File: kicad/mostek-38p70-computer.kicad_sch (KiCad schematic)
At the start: 7 parts

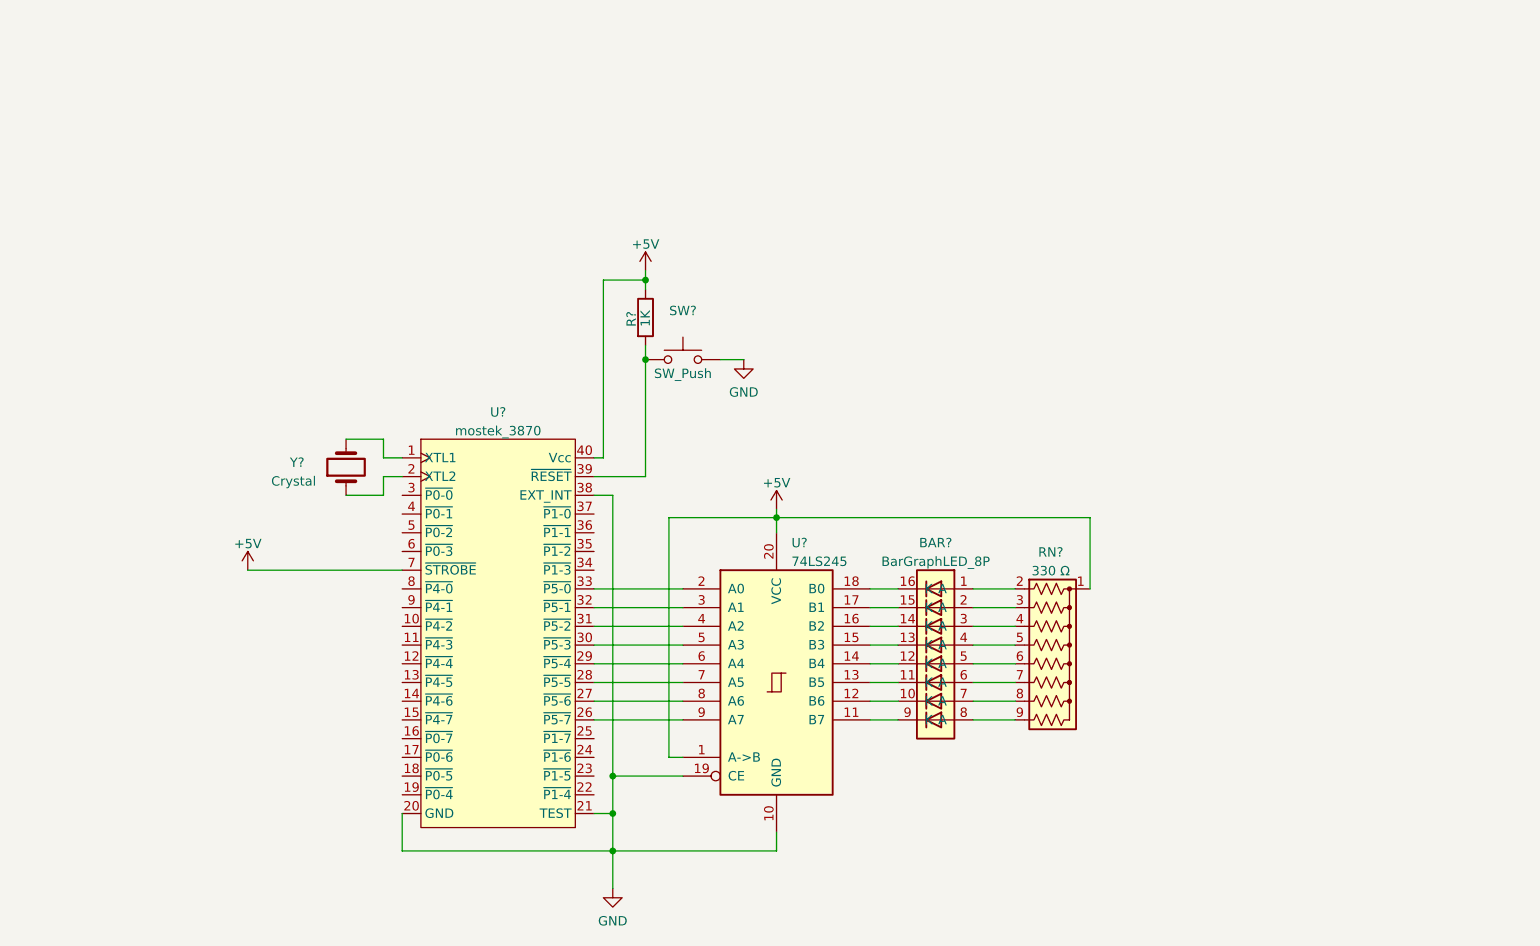
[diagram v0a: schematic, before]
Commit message: added switch inputs
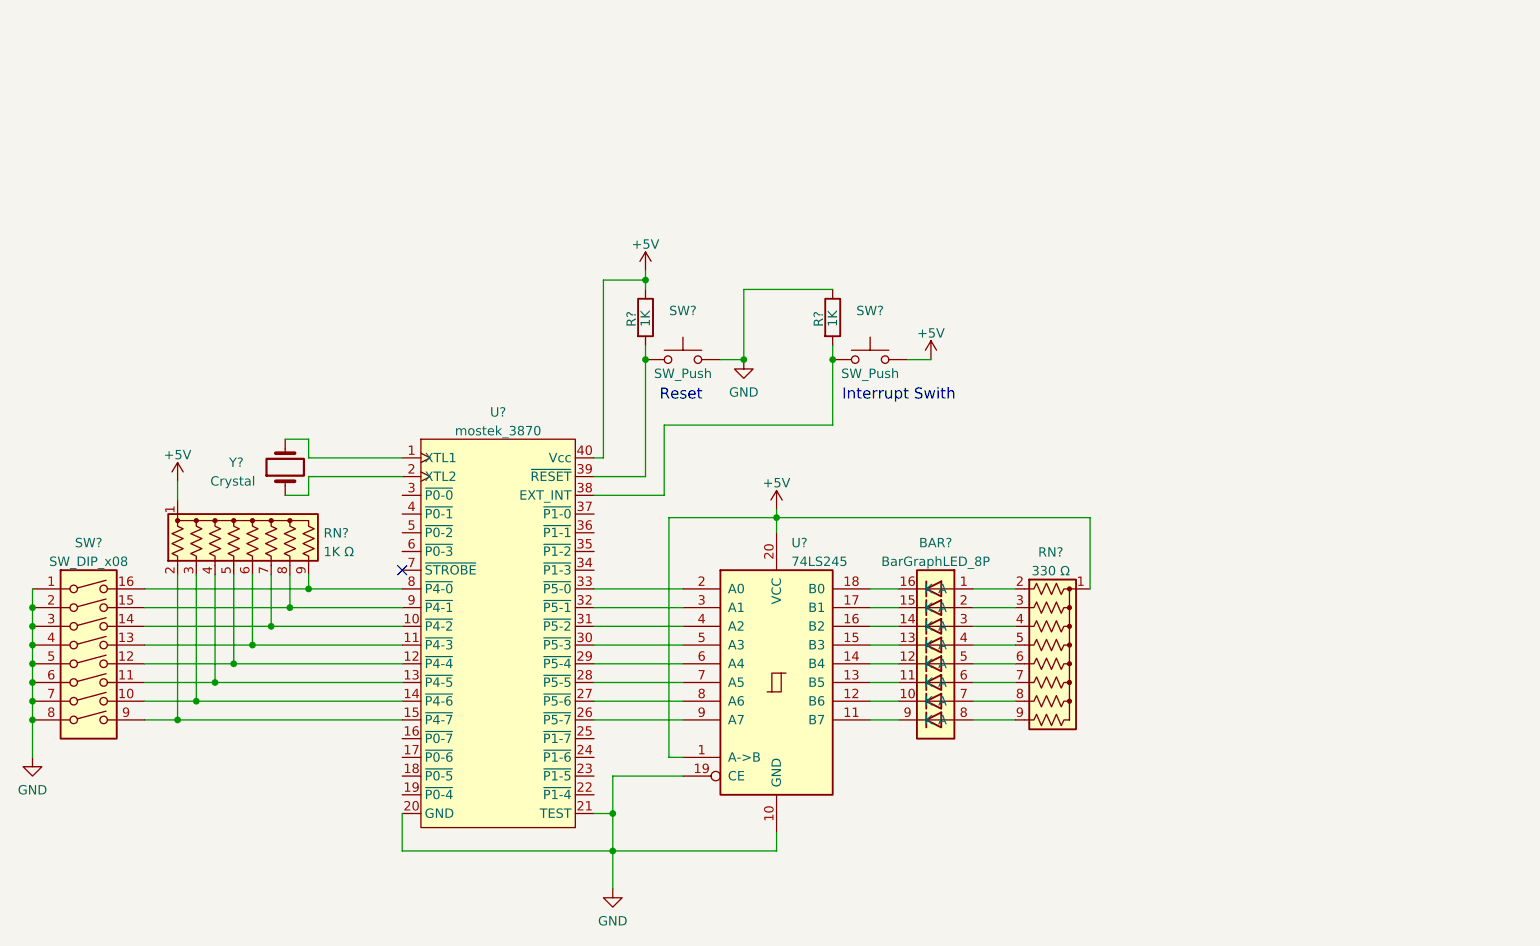
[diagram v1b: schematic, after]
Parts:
- added R?: 1K, symbol Device:R
- added RN?: 1K Ω, Resistor_THT:R_Array_SIP9, symbol Device:R_Network08_US
- added SW?: SW_DIP_x08, symbol Switch:SW_DIP_x08
- added SW?: SW_Push, symbol Switch:SW_Push
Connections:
- net +5V: now also RN?.1 (common), SW?.2; no longer U?.7 (~{STROBE})
- net GND: now also R?.1, SW?.1, SW?.2, SW?.3, SW?.4, SW?.5, SW?.6, SW?.7, SW?.8; no longer U?.38 (EXT_INT)
- net at U?.10 (~{P4-2}): now also RN?.7 (R6), SW?.14
- net at U?.11 (~{P4-3}): now also RN?.6 (R5), SW?.13
- net at U?.12 (~{P4-4}): now also RN?.5 (R4), SW?.12
- net at U?.13 (~{P4-5}): now also RN?.4 (R3), SW?.11
- net at U?.14 (~{P4-6}): now also RN?.3 (R2), SW?.10
- net at U?.15 (~{P4-7}): now also RN?.2 (R1), SW?.9
- net at U?.8 (~{P4-0}): now also RN?.9 (R8), SW?.16
- net at U?.9 (~{P4-1}): now also RN?.8 (R7), SW?.15
- new net: R?.2, SW?.1, U?.38 (EXT_INT)
- no-connect marks 0 -> 1
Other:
- note added: "Interrupt Swith"
- note added: "Reset"
- moved on the sheet: Y?

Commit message: added keypad to schematic
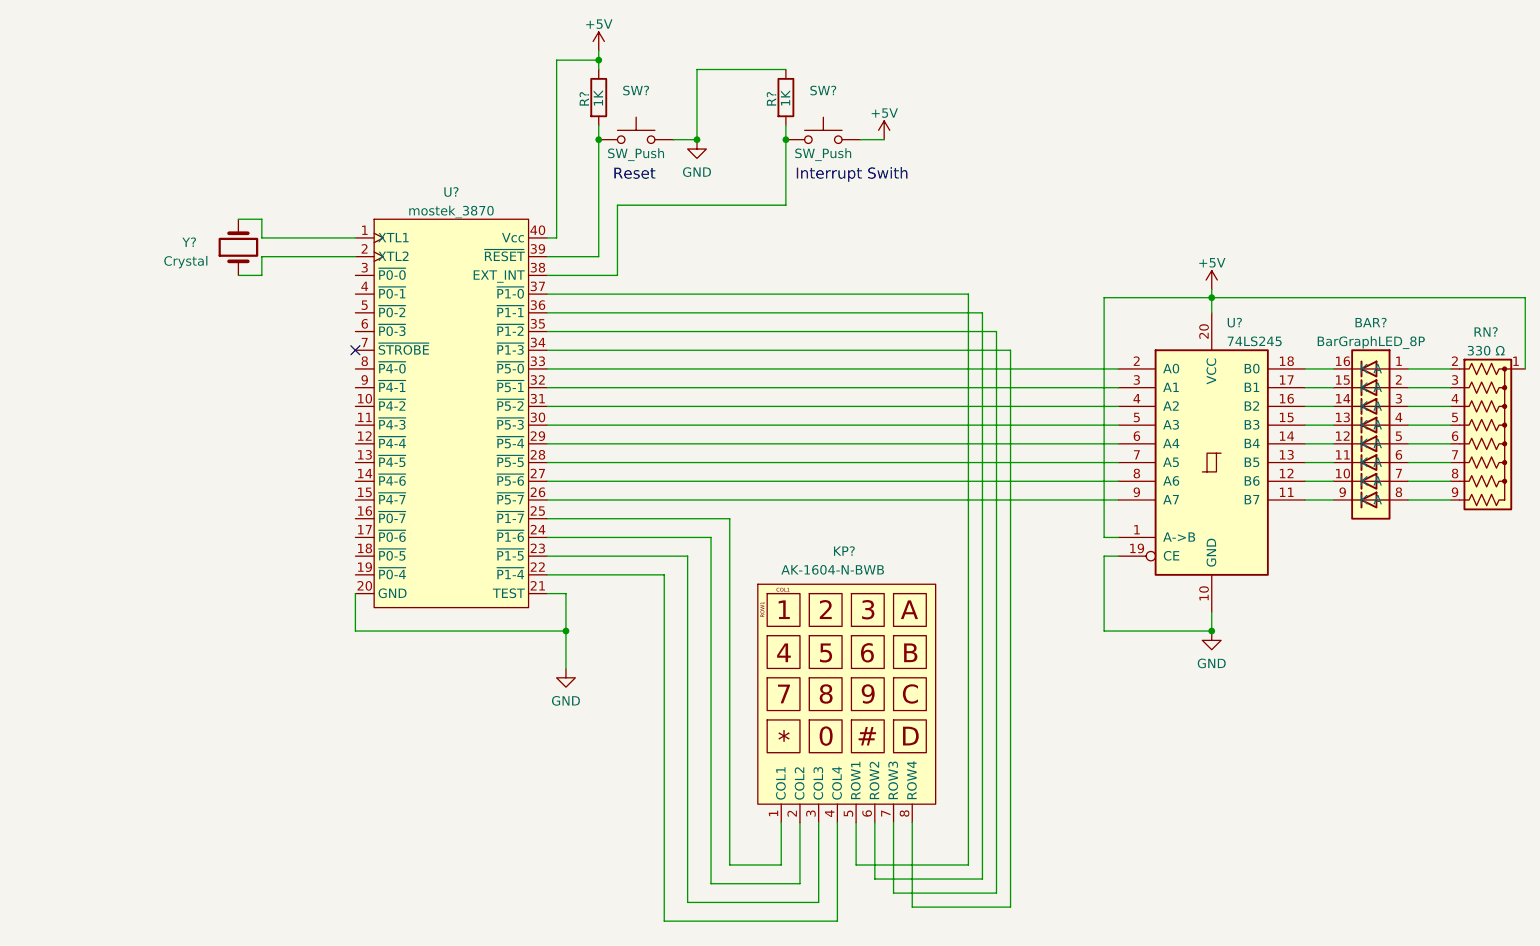
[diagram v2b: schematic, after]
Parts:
- removed RN?: 1K Ω, Resistor_THT:R_Array_SIP9, symbol Device:R_Network08_US
- removed SW?: SW_DIP_x08, symbol Switch:SW_DIP_x08
- added KP?: AK-1604-N-BWB, symbol ak_1604_keypad:AK-1604-N-BWB
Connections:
- net at U?.22 (~{P1-4}): now also KP?.4 (COL4)
- net at U?.23 (~{P1-5}): now also KP?.3 (COL3)
- net at U?.24 (~{P1-6}): now also KP?.2 (COL2)
- net at U?.25 (~{P1-7}): now also KP?.1 (COL1)
- net at U?.34 (~{P1-3}): now also KP?.8 (ROW4)
- net at U?.35 (~{P1-2}): now also KP?.7 (ROW3)
- net at U?.36 (~{P1-1}): now also KP?.6 (ROW2)
- net at U?.37 (~{P1-0}): now also KP?.5 (ROW1)
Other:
- moved on the sheet: BAR?, R?, RN?, SW?, U?, Y?

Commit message: added support for a keypad
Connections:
- net at KP?.1 (COL1): now also U?.22 (~{P1-4}); no longer U?.25 (~{P1-7})
- net at KP?.2 (COL2): now also U?.23 (~{P1-5}); no longer U?.24 (~{P1-6})
- net at KP?.3 (COL3): now also U?.24 (~{P1-6}); no longer U?.23 (~{P1-5})
- net at KP?.4 (COL4): now also U?.25 (~{P1-7}); no longer U?.22 (~{P1-4})
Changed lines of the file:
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@@
     (stroke (width 0) (type default) (color 0 0 0 0))
   )
-  (wire (pts (xy 160.655 130.81) (xy 167.64 130.81))
+  (wire (pts (xy 160.655 130.81) (xy 175.26 130.81))
     (stroke (width 0) (type default) (color 0 0 0 0))
   )
@@
     (stroke (width 0) (type default) (color 0 0 0 0))
   )
+  (wire (pts (xy 172.72 133.35) (xy 172.72 125.095))
+    (stroke (width 0) (type default) (color 0 0 0 0))
+  )
   (wire (pts (xy 252.73 81.28) (xy 258.445 81.28))
     (stroke (width 0) (type default) (color 0 0 0 0))
@@
     (stroke (width 0) (type default) (color 0 0 0 0))
   )
-  (wire (pts (xy 151.765 138.43) (xy 175.26 138.43))
+  (wire (pts (xy 167.64 138.43) (xy 167.64 125.095))
     (stroke (width 0) (type default) (color 0 0 0 0))
   )
@@
     (stroke (width 0) (type default) (color 0 0 0 0))
   )
+  (wire (pts (xy 154.94 135.89) (xy 170.18 135.89))
+    (stroke (width 0) (type default) (color 0 0 0 0))
+  )
   (wire (pts (xy 137.16 45.72) (xy 137.16 21.59))
     (stroke (width 0) (type default) (color 0 0 0 0))
@@
     (stroke (width 0) (type default) (color 0 0 0 0))
   )
-  (wire (pts (xy 154.94 135.89) (xy 172.72 135.89))
-    (stroke (width 0) (type default) (color 0 0 0 0))
-  )
   (wire (pts (xy 198.755 136.525) (xy 185.42 136.525))
     (stroke (width 0) (type default) (color 0 0 0 0))
@@
     (stroke (width 0) (type default) (color 0 0 0 0))
   )
+  (wire (pts (xy 170.18 135.89) (xy 170.18 125.095))
+    (stroke (width 0) (type default) (color 0 0 0 0))
+  )
   (wire (pts (xy 213.36 88.9) (xy 211.455 88.9))
     (stroke (width 0) (type default) (color 0 0 0 0))
@@
     (stroke (width 0) (type default) (color 0 0 0 0))
   )
-  (wire (pts (xy 170.18 133.35) (xy 170.18 125.095))
-    (stroke (width 0) (type default) (color 0 0 0 0))
-  )
   (wire (pts (xy 138.43 99.06) (xy 138.43 104.14))
     (stroke (width 0) (type default) (color 0 0 0 0))
@@
     (stroke (width 0) (type default) (color 0 0 0 0))
   )
-  (wire (pts (xy 158.115 133.35) (xy 170.18 133.35))
-    (stroke (width 0) (type default) (color 0 0 0 0))
-  )
   (wire (pts (xy 145.415 41.275) (xy 168.275 41.275))
     (stroke (width 0) (type default) (color 0 0 0 0))
   )
+  (wire (pts (xy 158.115 133.35) (xy 172.72 133.35))
+    (stroke (width 0) (type default) (color 0 0 0 0))
+  )
   (wire (pts (xy 193.04 130.81) (xy 177.8 130.81))
     (stroke (width 0) (type default) (color 0 0 0 0))
@@
     (stroke (width 0) (type default) (color 0 0 0 0))
   )
-  (wire (pts (xy 172.72 135.89) (xy 172.72 125.095))
-    (stroke (width 0) (type default) (color 0 0 0 0))
-  )
   (wire (pts (xy 135.89 81.28) (xy 213.36 81.28))
     (stroke (width 0) (type default) (color 0 0 0 0))
@@
     (stroke (width 0) (type default) (color 0 0 0 0))
   )
-  (wire (pts (xy 175.26 138.43) (xy 175.26 125.095))
-    (stroke (width 0) (type default) (color 0 0 0 0))
-  )
   (wire (pts (xy 226.06 52.705) (xy 226.06 53.827))
     (stroke (width 0) (type default) (color 0 0 0 0))
   )
-  (wire (pts (xy 167.64 130.81) (xy 167.64 125.095))
-    (stroke (width 0) (type default) (color 0 0 0 0))
-  )
   (wire (pts (xy 178.435 32.385) (xy 181.61 32.385))
     (stroke (width 0) (type default) (color 0 0 0 0))
@@
     (stroke (width 0) (type default) (color 0 0 0 0))
   )
+  (wire (pts (xy 151.765 138.43) (xy 167.64 138.43))
+    (stroke (width 0) (type default) (color 0 0 0 0))
+  )
   (wire (pts (xy 153.035 32.385) (xy 156.21 32.385))
     (stroke (width 0) (type default) (color 0 0 0 0))
@@
     (stroke (width 0) (type default) (color 0 0 0 0))
   )
+  (wire (pts (xy 175.26 130.81) (xy 175.26 125.095))
+    (stroke (width 0) (type default) (color 0 0 0 0))
+  )
